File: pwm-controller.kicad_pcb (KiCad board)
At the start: 4 copper layers, 50 x 50 mm, 64 parts, among them J1 DEBUG_ADDRESS_I2C_INT, J2 POWER, J3 OUT+, J4 OUT-, Q1 MMBT5551, Q10 MMBT5551, Q2 SiS402DN, Q3 SiS402DN, Q4 MMBT5401, Q5 MMBT5551, Q6 SiS402DN, Q7 SiS402DN, Q8 MMBT5401, Q9 MMBT5551, SW1 EC12D1524403, U1 STM8S003F3Px, U2 78L05

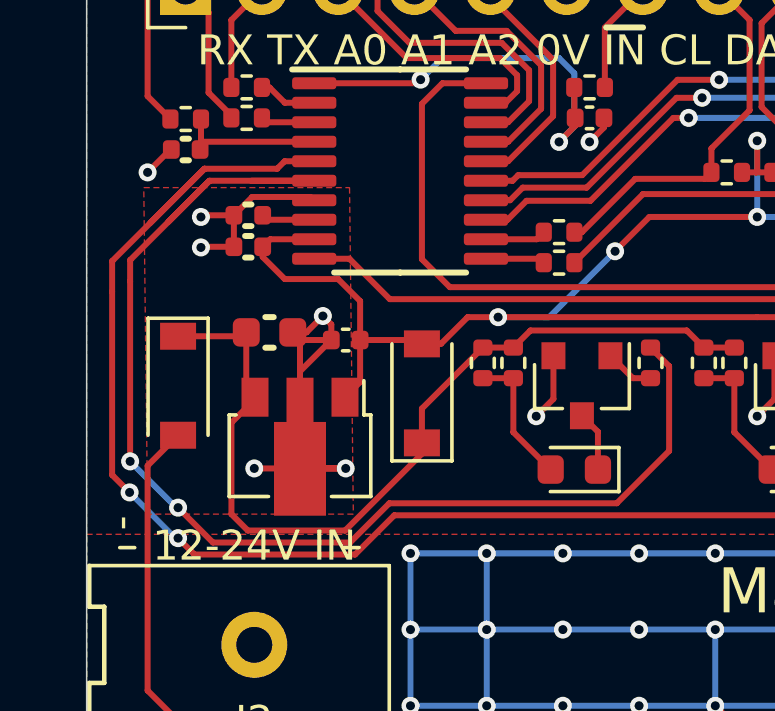
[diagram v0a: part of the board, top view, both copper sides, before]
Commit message: added some fills
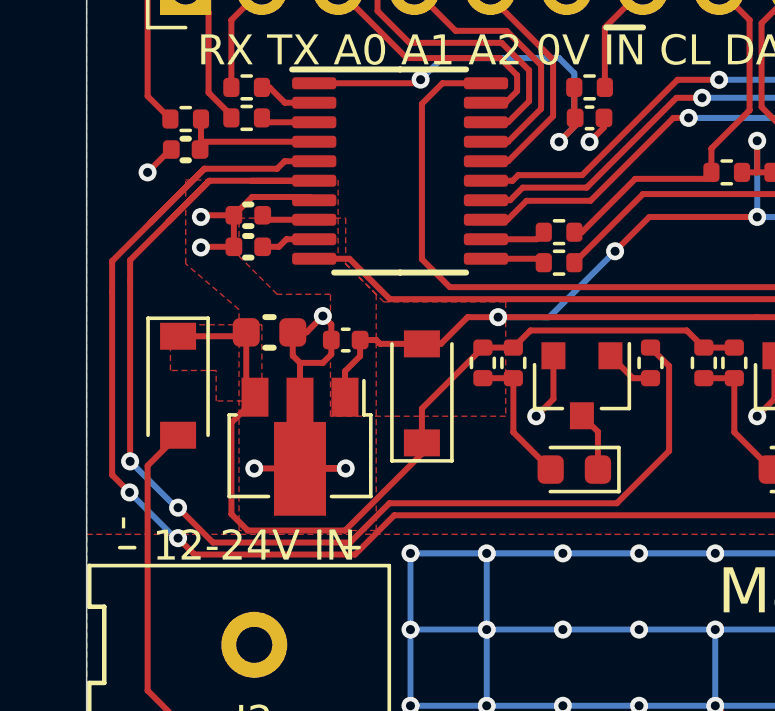
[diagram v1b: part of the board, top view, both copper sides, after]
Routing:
- net +5V: track 76.5 -> 71.0 mm
- net GND: track 181.8 -> 179.6 mm
- added copper zone on F.Cu, net +5V
- added copper zone on F.Cu, net VIN_D
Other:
- board text added: "DIMMER SWITCHES!"

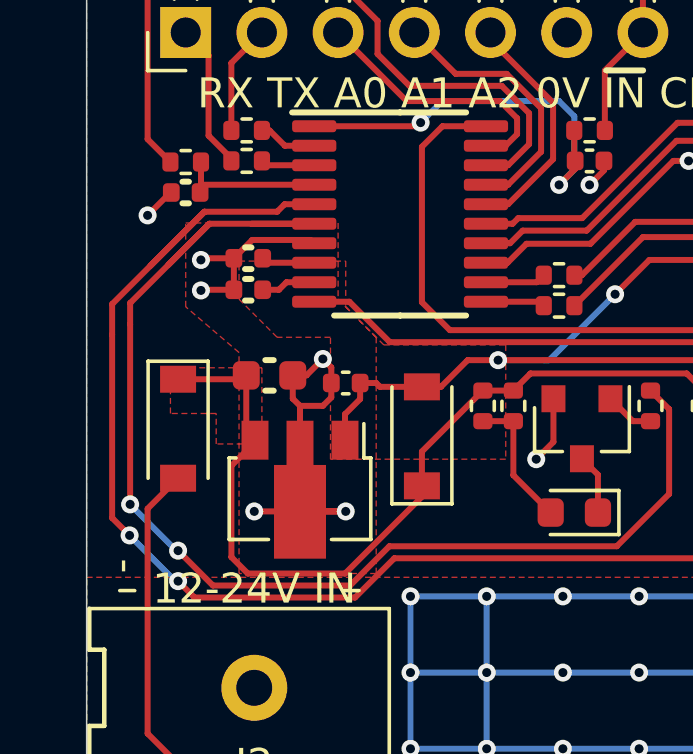
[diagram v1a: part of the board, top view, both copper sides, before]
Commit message: Fixed VCAP (3.3nF should be 470...3300nF)
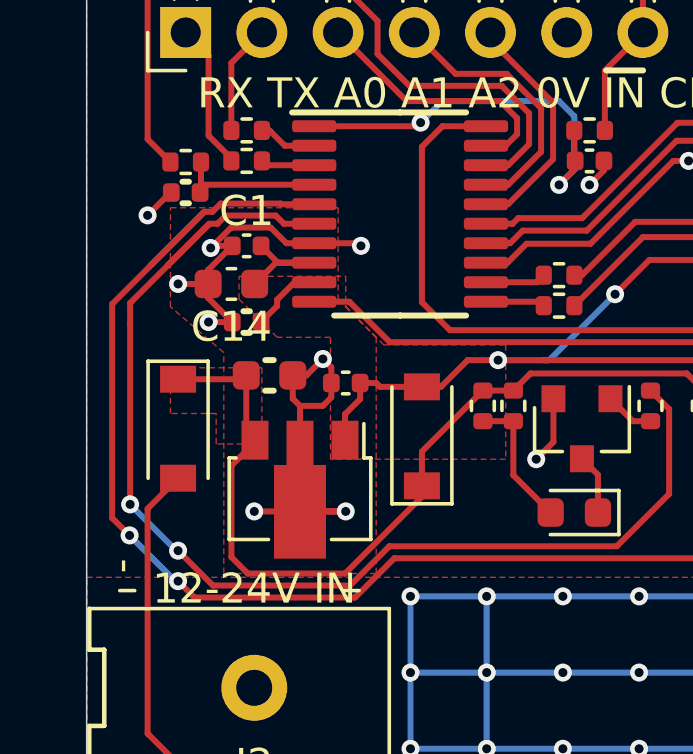
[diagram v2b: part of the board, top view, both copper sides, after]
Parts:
- added C14: 1u/50, Capacitor_SMD:C_0603_1608Metric, F.Cu at (81.0, 91.2)
- C1: value 3.3n -> 100n
- moved C2 1.08 mm to (81.5, 92.5)
- moved C1 0.42 mm to (81.5, 89.9), turned to 0 degrees
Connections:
- C1 pad 1: Net-(C1-Pad1) -> GND
- C1 pad 2: GND -> /VCAP
- U1 pad 8: Net-(C1-Pad1) -> /VCAP
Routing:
- net GND: track 179.6 -> 184.6 mm, vias 63 -> 65
- net /VCAP: track 0.00 -> 4.28 mm
- net LED2: track 42.0 -> 40.2 mm
- net Net-(C1-Pad1): track 1.78 -> 0.00 mm
- net +5V: track 71.0 -> 71.6 mm

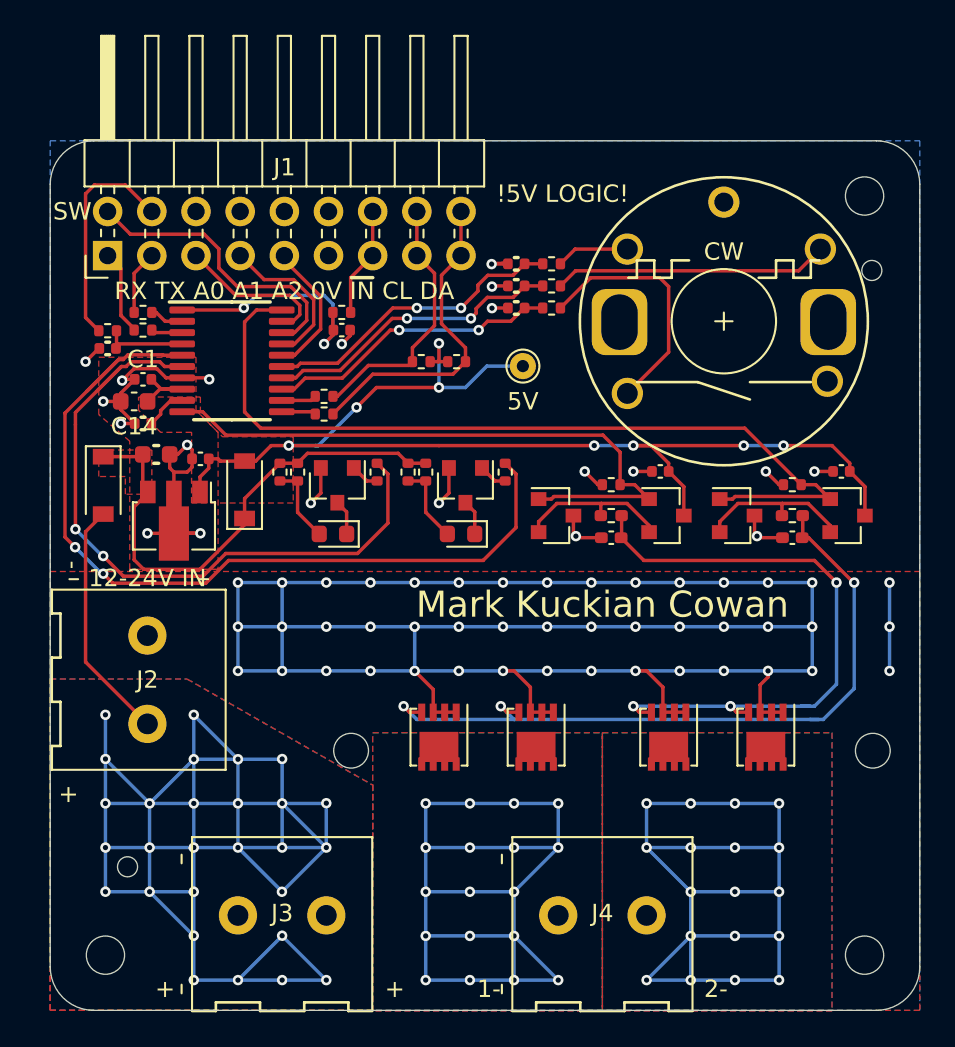
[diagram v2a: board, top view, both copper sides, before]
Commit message: migrated to Kicad v6, fixed a bunch of DRC issues
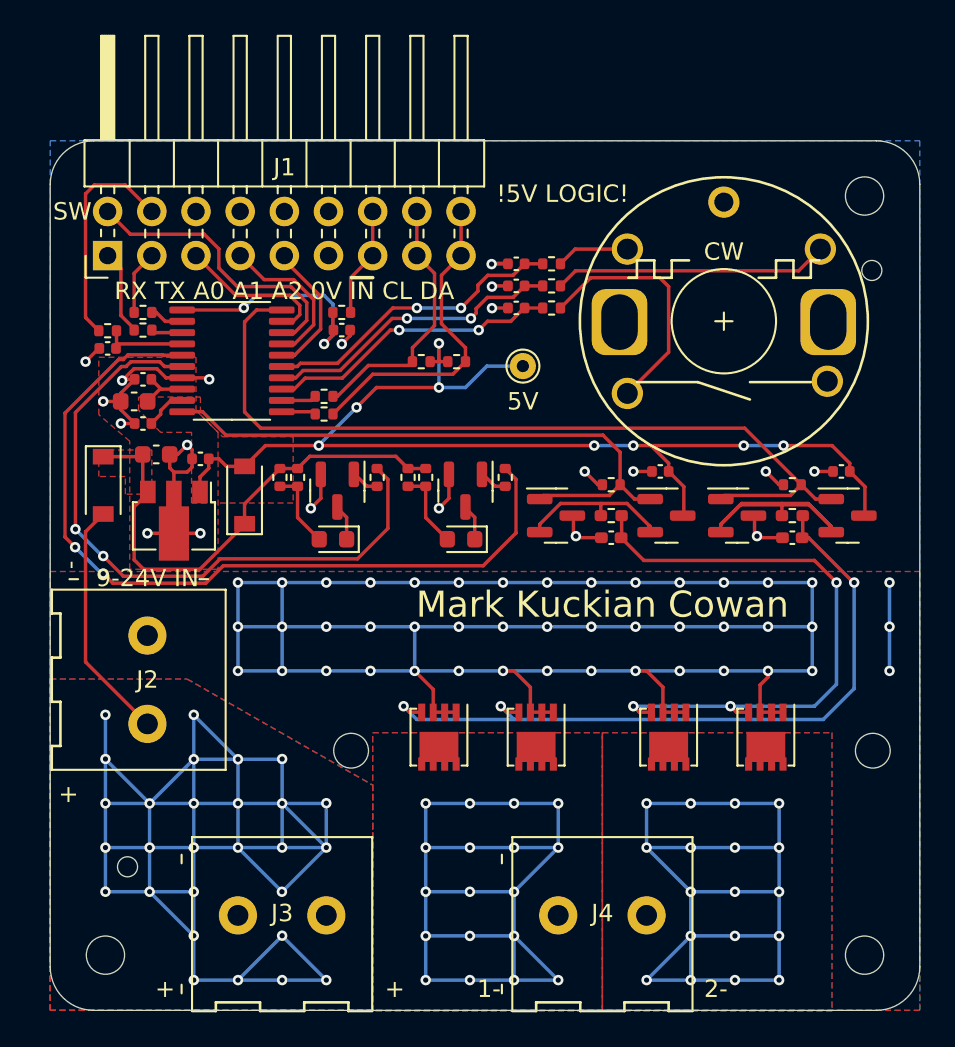
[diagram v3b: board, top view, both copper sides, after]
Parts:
- moved D1 0.30 mm to (87.4, 96.6)
- moved D3 0.30 mm to (99.8, 99.1)
- moved D4 0.30 mm to (92.5, 99.1)
- moved Q10 0.30 mm to (100.1, 96.3)
- moved Q9 0.30 mm to (92.7, 96.3)
- moved R15 0.30 mm to (95.0, 95.6)
- moved R16 0.30 mm to (89.4, 95.6)
- moved R17 0.30 mm to (90.4, 95.6)
- moved R18 0.30 mm to (102.4, 95.6)
- moved R19 0.30 mm to (96.8, 95.6)
- moved R20 0.30 mm to (97.8, 95.6)
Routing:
- net Net-(Q5-Pad2): track 9.00 -> 16.5 mm
- net LED1: track 50.1 -> 47.4 mm
- net +5V: track 71.6 -> 69.0 mm
- net LED2: track 40.2 -> 38.1 mm
- net GND: track 184.6 -> 182.6 mm
- net PWM2: track 50.1 -> 48.4 mm
- net PWM1: track 36.5 -> 35.0 mm
- net /VCAP: track 4.28 -> 3.07 mm
- net SADD0: track 9.54 -> 8.89 mm
- net SADD1: track 9.56 -> 9.01 mm
- net /channel1/GATE: track 35.6 -> 35.1 mm
- net /channel2/GATE: track 42.3 -> 41.8 mm
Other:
- net class Default removed

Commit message: order files
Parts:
- renumbered C4 to C1, C14 to C10, C10 to C11, C11 to C12, C12 to C13, C13 to C14, C5 to C2, C7 to C4, C8 to C5, C9 to C6, C2 to C7, C1 to C8, C6 to C9, D2 to D1, D1 to D2, H4 to H2, H2 to H3, H5 to H4, H7 to H5, H3 to H6, H6 to H7, J2 to J1, J1 to J2, Q4 to Q2, Q2 to Q3, Q3 to Q4, Q8 to Q6, Q6 to Q7, Q7 to Q8, R8 to R1, R7 to R10, R21 to R11, R11 to R13, R13 to R15, R15 to R18, R10 to R2, R18 to R21, R5 to R4, R9 to R5, R1 to R6, R2 to R7, R4 to R8, R6 to R9, U2 to U1, U1 to U2

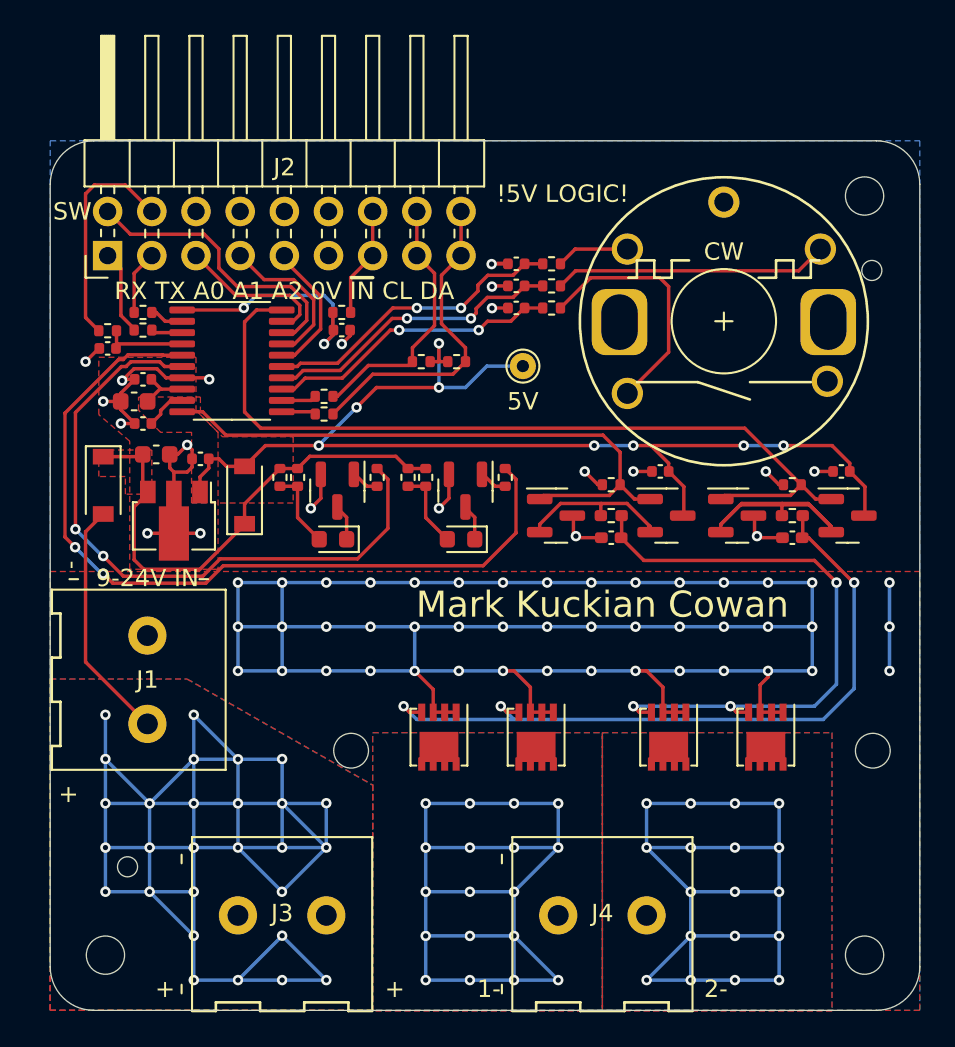
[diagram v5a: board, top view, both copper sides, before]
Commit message: fix rotary pinout, add 5v0 to header in extra-col, regen fab+doc
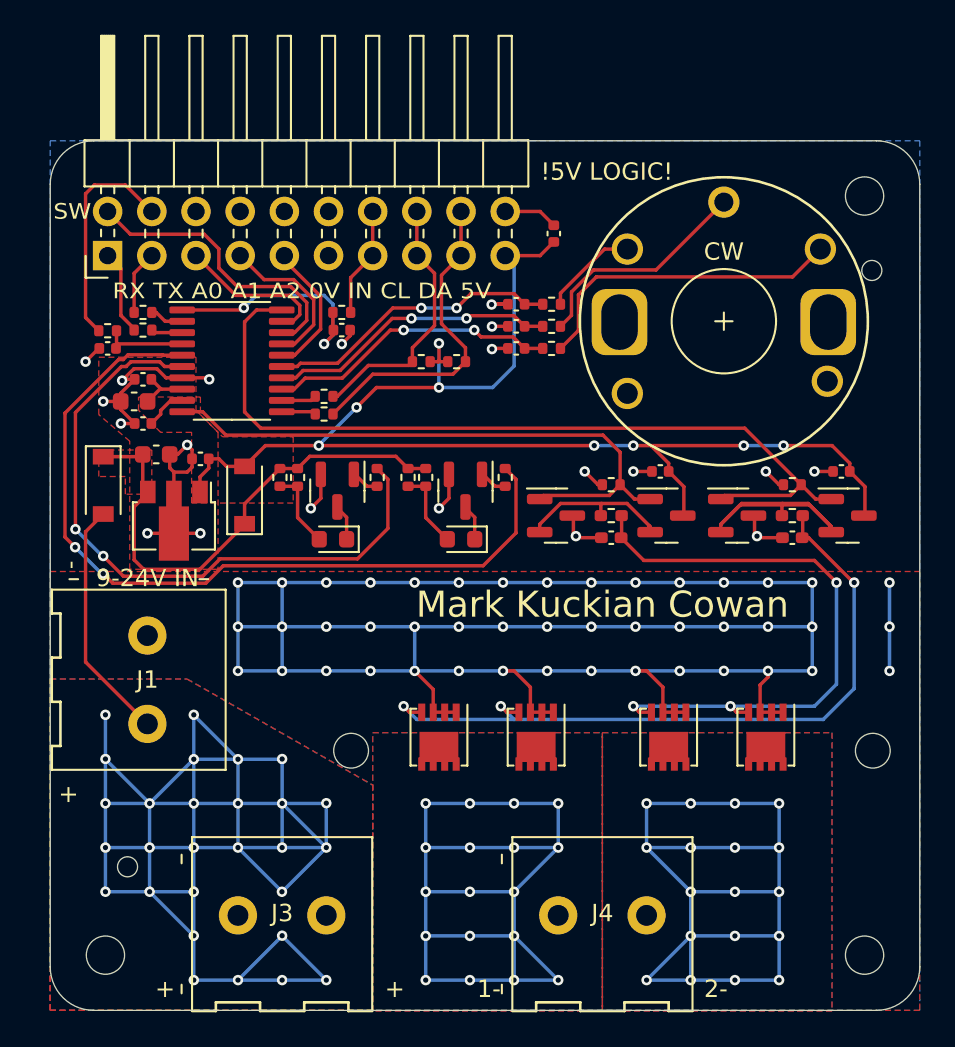
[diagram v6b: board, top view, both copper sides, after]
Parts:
- removed TP1: 5V, TestPoint:TestPoint_THTPad_D1.5mm_Drill0.7mm
- added C7: 100n, Capacitor_SMD:C_0402_1005Metric, F.Cu at (105.2, 81.5)
- J2: value DEBUG_ADDRESS_I2C_INT -> DEBUG_ADDRESS_I2C_INT_5V; footprint Connector_PinHeader_2.54mm:PinHeader_2x09_P2.54mm_Horizontal -> Connector_PinHeader_2.54mm:PinHeader_2x10_P2.54mm_Horizontal
- moved C5 3.59 mm to (103.0, 88.1)
- moved R2 3.59 mm to (105.0, 88.1)
- moved C4 2.32 mm to (103.0, 85.6)
- moved R1 2.32 mm to (105.0, 85.6)
- moved C6 1.05 mm to (103.0, 86.9)
- moved R5 1.05 mm to (105.0, 86.9)
- renumbered C9 to C10, C10 to C11, C11 to C12, C12 to C13, C13 to C14, C14 to C15, C7 to C8, C8 to C9
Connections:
- U2 pad 13: RE_B -> RE_Q
- U2 pad 14: RE_Q -> RE_B
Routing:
- net +5V: track 69.0 -> 78.2 mm
- net GND: track 182.6 -> 185.7 mm
- net Net-(R2-Pad1): track 15.8 -> 18.5 mm
- net Net-(R1-Pad1): track 4.20 -> 5.53 mm
- net Net-(R5-Pad2): track 14.3 -> 13.1 mm
- net RE_I: track 17.7 -> 17.0 mm
- net RE_Q: track 17.4 -> 16.9 mm
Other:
- board text added: "RX TX A0 A1 A2 0V IN CL DA 5V"
- board text added: "SW"

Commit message: TVS diodes added to I2C SDA+SCL+INT pins, renamed 1-/2- to A-/B-
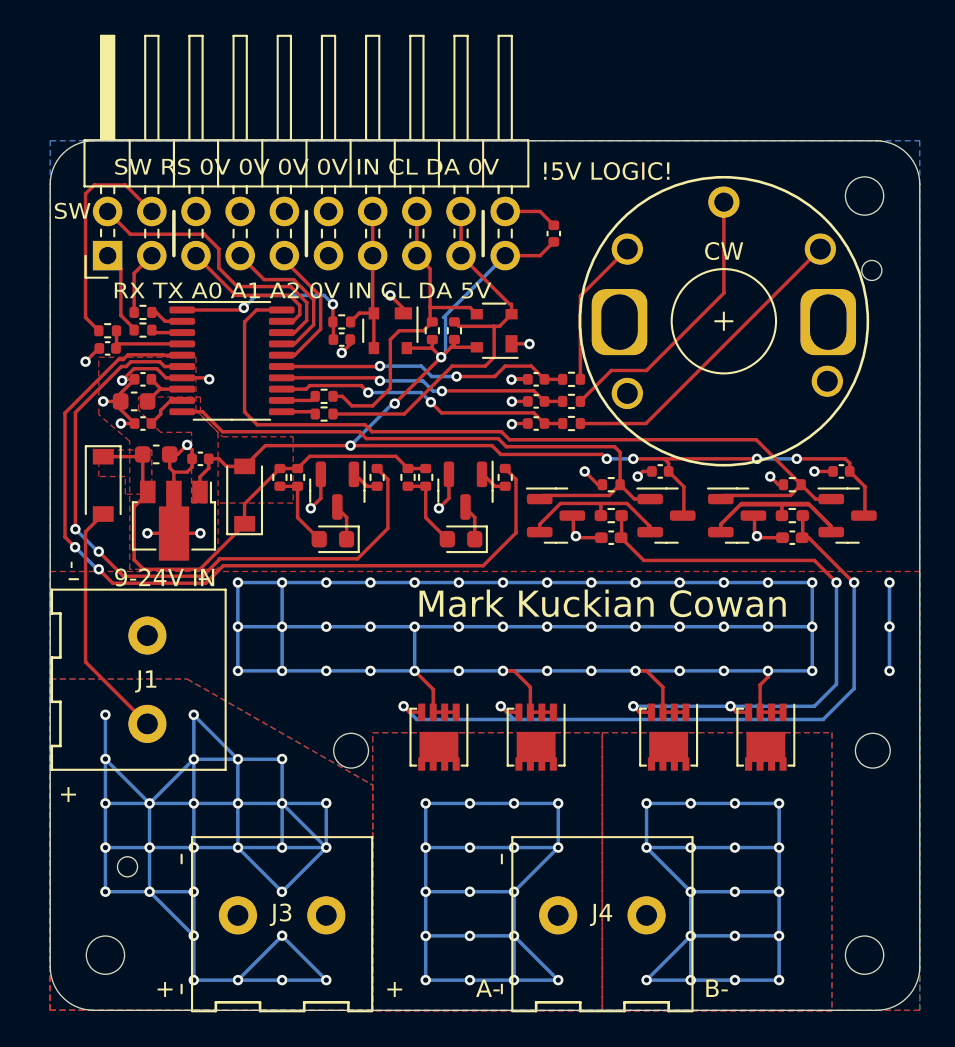
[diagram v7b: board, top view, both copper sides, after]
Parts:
- added U3: DRTR5V0U2SR, Package_TO_SOT_SMD:SOT-143, F.Cu at (101.7, 87.1)
- added U4: DRTR5V0U2SR, Package_TO_SOT_SMD:SOT-143, F.Cu at (95.8, 87.1)
- moved R5 4.47 mm to (106.2, 91.2)
- moved C6 4.47 mm to (104.1, 91.2)
- moved R1 4.47 mm to (106.2, 89.9)
- moved R2 4.47 mm to (106.2, 92.5)
- moved C4 4.47 mm to (104.1, 89.9)
- moved C5 4.47 mm to (104.1, 92.5)
- moved R3 1.89 mm to (98.2, 87.1), turned to -90 degrees
- moved R4 1.78 mm to (99.4, 87.1), turned to -90 degrees
- moved R8 0.55 mm to (93.0, 86.6)
- moved C3 0.55 mm to (93.0, 87.6)
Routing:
- net +5V: track 78.2 -> 72.9 mm, vias 8 -> 7
- net SDA: track 18.5 -> 23.1 mm
- net SCL: track 15.0 -> 19.1 mm
- net INT: track 6.33 -> 9.41 mm
- net Net-(R1-Pad1): track 5.53 -> 8.61 mm
- net Net-(R5-Pad2): track 13.1 -> 16.1 mm
- net /INT_PIN: track 13.8 -> 11.3 mm
- net GND: track 185.7 -> 187.6 mm, vias 65 -> 67
- net Net-(R2-Pad1): track 18.5 -> 18.0 mm
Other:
- board text added: "SW RS 0V 0V 0V 0V IN CL DA 0V"

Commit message: improvements, notes for future TODO stuff
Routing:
- net VIN: track 132.7 -> 14.0 mm, vias 28 -> 14
- net DRAIN1: track 58.0 -> 0.00 mm, vias 18 -> 9
- net DRAIN2: track 58.0 -> 0.00 mm, vias 18 -> 9
- net GND: vias 67 -> 99
